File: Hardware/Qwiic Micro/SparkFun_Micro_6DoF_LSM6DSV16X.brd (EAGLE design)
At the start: 19.1 x 7.6 mm, 42 parts, among them J1 Qwiic Right Angle, U2 LSM6DSV16X

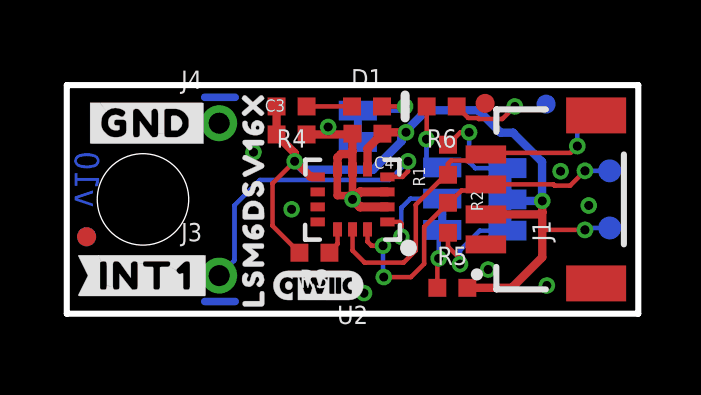
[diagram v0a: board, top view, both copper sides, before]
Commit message: Increases pad size, decreases paste size on footprint
* Also adds trestrict between ground pads to the footprint itself
* Fixes gyro silk on bottom
* Swaps PICO and CS on 1x1 header
* Improves ground pour
* Adds more notes to the filter section
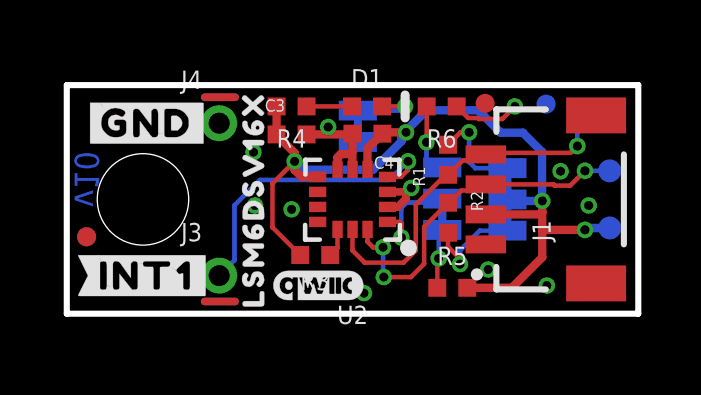
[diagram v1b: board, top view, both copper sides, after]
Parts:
- R4: value 1k -> 2.2k
- moved R3 0.08 mm to (8.28, 1.96)
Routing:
- net GND: track 13.0 -> 11.9 mm, vias 10 -> 11
